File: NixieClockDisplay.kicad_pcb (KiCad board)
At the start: 2 copper layers, 160 x 65 mm, 61 parts, among them J1 CONN_01X08, J2 CONN_01X03, J3 CONN_01X03, J4 CONN_02X04, J5 CONN_01X02, U1 TPIC6B595, U2 TPIC6B595, U3 TPIC6B595, U4 TPIC6B595, U5 TPIC6B595, U6 TPIC6B595, U7 WE-FDSM_DC/DC_5V

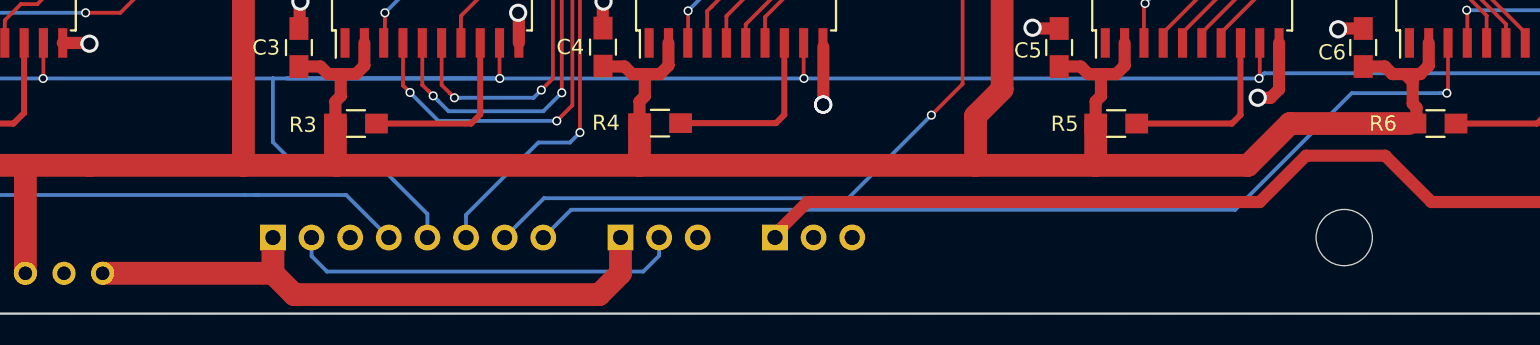
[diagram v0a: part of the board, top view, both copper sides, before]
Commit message: Arranged connectors to mate with NixiePowerSupply board.
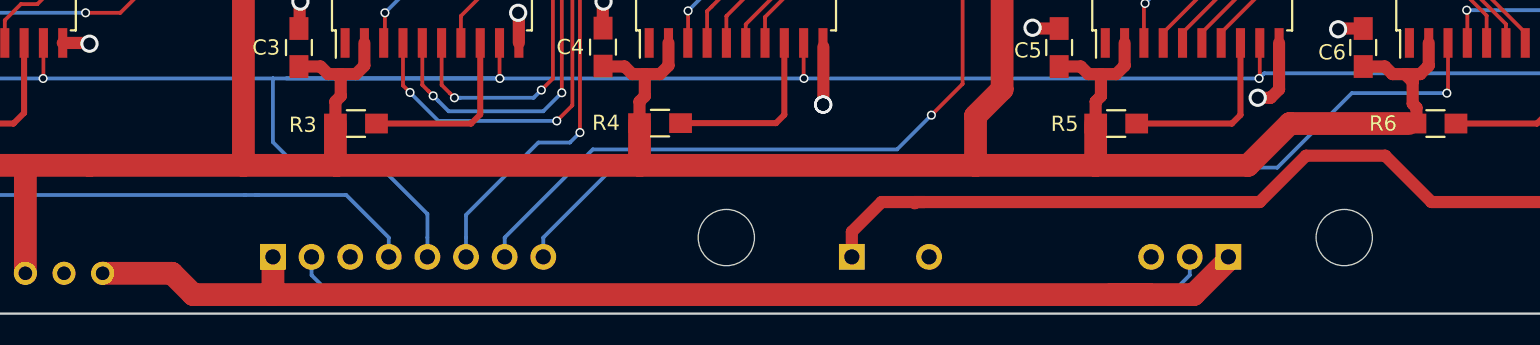
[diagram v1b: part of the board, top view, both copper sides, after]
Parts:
- added REF**: MountingHole_3.7mm, Mounting_Holes:MountingHole_3.7mm, F.Cu at (159.4, 100.0)
- J3: value CONN_01X03 -> CONN_01X02; footprint Pin_Headers:Pin_Header_Straight_1x03_Pitch2.54mm -> NixieClockDisplay:Pin_Header_Straight_1x03_Pitch2.54mm_No_Center
- moved J2 40.0 mm to (192.4, 101.3), turned to 90 degrees
- moved J3 5.21 mm to (167.6, 101.3)
- moved J1 1.27 mm to (129.5, 101.3)
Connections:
- J3 pad 2: Net-(J3-Pad2) -> GND
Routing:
- net +12V: track 39.9 -> 80.7 mm
- net /SHDN: track 26.1 -> 61.7 mm
- net /HV: track 325.0 -> 322.1 mm
- net Net-(J1-Pad8): track 66.7 -> 68.0 mm
- net /PIXEL_IN: track 101.9 -> 103.1 mm
- net /SRCK: track 182.1 -> 183.3 mm
- net /RCK: track 160.4 -> 161.7 mm
- net //G: track 166.2 -> 167.5 mm

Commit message: Final board.
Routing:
- net GND: track 155.5 -> 162.4 mm
- net Net-(LED2-Pad1): track 16.6 -> 14.0 mm
- net Net-(LED6-Pad1): track 16.3 -> 14.0 mm
- net Net-(LED1-Pad1): track 20.3 -> 18.4 mm
- net Net-(LED5-Pad1): track 20.2 -> 18.9 mm
- net Net-(LED10-Pad3): track 19.9 -> 18.7 mm
- net Net-(LED8-Pad1): track 16.2 -> 16.9 mm
- net Net-(LED4-Pad1): track 16.2 -> 16.9 mm
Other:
- board text added: "HV /EN"
- board text added: "NIXIE /EN"
- board text removed: "ENABLE"

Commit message: Begin layout
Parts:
- removed J1: CONN_01X08, Pin_Headers:Pin_Header_Straight_1x08_Pitch2.54mm
- removed the REF** at (159.4, 100.0)
- added C17: .01uF, Capacitors_SMD:C_0805_HandSoldering, F.Cu at (114.1, 99.5)
- added C18: .01uF, Capacitors_SMD:C_0805_HandSoldering, F.Cu at (106.7, 99.8)
- added C19: .1uF, Capacitors_SMD:C_0805_HandSoldering, F.Cu at (136.5, 107.0)
- added C20: .01uF, Capacitors_SMD:C_0805_HandSoldering, F.Cu at (120.2, 100.0)
- added R14: 10K, Resistors_SMD:R_0805_HandSoldering, F.Cu at (161.2, 98.8)
- added R15: 10K, Resistors_SMD:R_0805_HandSoldering, F.Cu at (161.2, 105.2)
- added R16: 10K, Resistors_SMD:R_0805_HandSoldering, F.Cu at (117.1, 99.7)
- added R17: 10K, Resistors_SMD:R_0805_HandSoldering, F.Cu at (109.4, 99.8)
- added R18: 10K, Resistors_SMD:R_0805_HandSoldering, F.Cu at (125.8, 100.0)
- added R19: 100, Resistors_SMD:R_0805_HandSoldering, F.Cu at (129.5, 100.0)
- added R20: 33R, Resistors_SMD:R_0805_HandSoldering, F.Cu at (135.0, 97.5)
- added R21: 10K, Resistors_SMD:R_0805_HandSoldering, F.Cu at (123.0, 100.0)
- added SW1: RotaryEncoder_Switch_RGB, NixieClockDisplay:EC12PLRGB_Rotary_Encoder, F.Cu at (150.0, 102.5)
- added U8: AdafruitProTrinket5V, NixieClockDisplay:Adafruit_Trinket_Pro, B.Cu at (150.0, 82.5)
- added U9: WS2811, Housings_SOIC:SOIC-8_3.9x4.9mm_Pitch1.27mm, F.Cu at (136.2, 102.1)
- J4: value CONN_02X04 -> Conn_02x02_Odd_Even; footprint Pin_Headers:Pin_Header_Straight_2x04_Pitch2.54mm -> Pin_Headers:Pin_Header_Straight_2x02_Pitch2.54mm
- J5: value CONN_01X02 -> Conn_01x04; footprint Pin_Headers:Pin_Header_Straight_1x02_Pitch2.54mm -> Pin_Headers:Pin_Header_Straight_1x04_Pitch2.54mm
- R10, R11, R12, R13, R8, R9: value 10K -> 22K
- moved U7 95.2 mm to (211.0, 97.5)
- moved C4 29.1 mm to (177.2, 74.5), turned to 180 degrees
- moved R4 21.5 mm to (176.5, 92.5)
- moved U3 21.0 mm to (119.0, 82.5), turned to 0 degrees
- moved U4 21.0 mm to (181.0, 82.5), turned to 0 degrees
- moved C5 18.4 mm to (194.2, 74.5), turned to 180 degrees
- moved C6 16.4 mm to (211.2, 74.5), turned to 180 degrees
- moved R1 11.2 mm to (76.2, 85.5), turned to 90 degrees
- moved C2 10.4 mm to (94.0, 80.0), turned to 90 degrees
- moved C1 9.01 mm to (76.2, 80.0), turned to 90 degrees
- moved U2 8.00 mm to (102.0, 82.5), turned to 0 degrees
- moved U5 8.00 mm to (198.0, 82.5), turned to 0 degrees
- moved R6 6.18 mm to (212.0, 91.0), turned to 180 degrees
- moved U1 5.00 mm to (85.0, 82.5), turned to 0 degrees
- moved U6 5.00 mm to (215.0, 82.5), turned to 0 degrees
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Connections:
- net /HV renamed Net-(J3-Pad1)
- J4 pad 1: /PIXEL_IN -> Net-(J4-Pad1)
- J4 pad 3: /RING_OUT -> +5V
- J4 pad 4: /RING_IN -> GND
- J5 pad 2: GND -> /TIME_IN
- N1 pad 8: Net-(N1-Pad8) -> /HOUR_40
- N1 pad 9: Net-(N1-Pad9) -> /HOUR_30
- R1 pad 1: +5V -> Net-(R1-Pad1)
- R1 pad 2: Net-(R1-Pad2) -> +5V
- R2 pad 1: +5V -> Net-(R2-Pad1)
- R2 pad 2: Net-(R2-Pad2) -> +5V
- R3 pad 1: +5V -> Net-(R3-Pad1)
- R3 pad 2: Net-(R3-Pad2) -> +5V
- R4 pad 1: +5V -> Net-(R4-Pad1)
- R4 pad 2: Net-(R4-Pad2) -> +5V
- R5 pad 1: +5V -> Net-(R5-Pad1)
- R5 pad 2: Net-(R5-Pad2) -> +5V
- R6 pad 1: +5V -> Net-(R6-Pad1)
- R6 pad 2: Net-(R6-Pad2) -> +5V
- R7 pad 2: Net-(J4-Pad2) -> Net-(R7-Pad2)
- U1 pad 16: Net-(U1-Pad16) -> /HOUR_30
- U1 pad 17: Net-(U1-Pad17) -> /HOUR_40
- U1 pad 8: Net-(R1-Pad2) -> Net-(R1-Pad1)
- U2 pad 8: Net-(R2-Pad2) -> Net-(R2-Pad1)
- U3 pad 8: Net-(R3-Pad2) -> Net-(R3-Pad1)
- U4 pad 8: Net-(R4-Pad2) -> Net-(R4-Pad1)
- U5 pad 8: Net-(R5-Pad2) -> Net-(R5-Pad1)
- U6 pad 8: Net-(R6-Pad2) -> Net-(R6-Pad1)
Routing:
- net +5V: track 532.5 -> 300.3 mm, vias 10 -> 8
- net /PIXEL_IN: track 103.1 -> 0.00 mm, vias 1 -> 0
- net /MIN_9: track 81.7 -> 0.00 mm, vias 2 -> 0
- net +12V: track 80.7 -> 0.00 mm
- net /MIN_8: track 75.9 -> 0.00 mm, vias 2 -> 0
- net /HOUR_9: track 73.4 -> 0.00 mm, vias 2 -> 0
- net /MIN_7: track 69.9 -> 0.00 mm, vias 2 -> 0
- net Net-(U6-Pad3): track 68.0 -> 0.00 mm, vias 1 -> 0
- net /HOUR_8: track 66.8 -> 0.00 mm, vias 2 -> 0
- net /SEC_60: track 65.6 -> 0.00 mm, vias 2 -> 0
- net /SHDN: track 61.7 -> 0.00 mm
- net /HOUR_7: track 60.9 -> 0.00 mm, vias 2 -> 0
- net /MIN_50: track 54.4 -> 0.00 mm, vias 2 -> 0
- net /SEC_8: track 50.6 -> 0.00 mm
- net /SEC_9: track 47.0 -> 0.00 mm, vias 2 -> 0
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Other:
- board size 160 x 65 mm -> 160 x 70 mm
- board text added: "DOUT to ring DIN Ring DOUT to DIN Short DOUT-DIN to omit ring"
- board text added: "TIME IN"
- board text removed: "1"
- board text removed: "2"
- board text removed: "3"
- board text removed: "HV /EN"
- board text removed: "NIXIE /EN"
- board text removed: "NIXIE DIN"
- board text removed: "PIXEL DIN"
- board text removed: "RCK"
- board text removed: "SRCK"
- board text removed: "Shunt 1-2 to omit ring Shunt 1-3 and 2-4 for ring DOUT to ring DIN Ring DOUT to DIN"

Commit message: More layout
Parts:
- moved C3 22.0 mm to (115.2, 74.5), turned to 180 degrees
- moved R3 18.9 mm to (115.5, 91.2), turned to 180 degrees
- moved R5 9.58 mm to (194.5, 91.2), turned to 180 degrees
- moved R1 7.79 mm to (81.5, 91.2), turned to 180 degrees
- moved R2 7.60 mm to (98.5, 91.2), turned to 180 degrees
- moved C1 7.43 mm to (81.2, 74.5), turned to 180 degrees
- moved C2 6.95 mm to (98.2, 74.5), turned to 180 degrees
- moved R4 1.56 mm to (177.5, 91.2), turned to 180 degrees
- moved R6 0.56 mm to (211.5, 91.2)
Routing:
- net +5V: track 300.3 -> 400.1 mm, vias 8 -> 18
- net /MIN_8: track 0.00 -> 86.1 mm, vias 0 -> 2
- net /MIN_9: track 0.00 -> 79.3 mm, vias 0 -> 2
- net Net-(U3-Pad3): track 0.00 -> 76.0 mm, vias 0 -> 2
- net /MIN_4: track 0.00 -> 69.1 mm, vias 0 -> 1
- net /MIN_5: track 0.00 -> 64.9 mm, vias 0 -> 1
- net /MIN_6: track 0.00 -> 56.3 mm, vias 0 -> 1
- net /MIN_3: track 0.00 -> 52.8 mm, vias 0 -> 1
- net /SEC_8: track 0.00 -> 51.2 mm, vias 0 -> 2
- net /SEC_60: track 0.00 -> 45.7 mm
- net /SEC_40: track 0.00 -> 45.5 mm
- net /SEC_9: track 0.00 -> 44.9 mm, vias 0 -> 2
- net /SEC_50: track 0.00 -> 44.3 mm
- net /MIN_2: track 0.00 -> 39.4 mm
- net /SEC_30: track 0.00 -> 38.1 mm
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
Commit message: More layout
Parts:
- moved C18 52.5 mm to (155.8, 81.0)
- moved R17 52.3 mm to (158.2, 81.0)
- moved C20 47.0 mm to (163.2, 81.0), turned to 270 degrees
- moved R21 42.3 mm to (160.8, 81.0), turned to 270 degrees
- moved C17 41.1 mm to (150.8, 81.0)
- moved R16 40.7 mm to (153.2, 81.0)
- moved C19 1.75 mm to (134.8, 107.0)
- moved R14 1.27 mm to (161.5, 100.0), turned to 180 degrees
- moved R15 0.35 mm to (161.5, 105.0), turned to 180 degrees
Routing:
- net +5V: track 400.1 -> 494.2 mm, vias 18 -> 23
- net /MIN_7: track 0.00 -> 83.3 mm, vias 0 -> 2
- net /MIN_50: track 0.00 -> 71.7 mm, vias 0 -> 3
- net /MIN_00: track 0.00 -> 49.9 mm, vias 0 -> 1
- net Net-(R15-Pad2): track 0.00 -> 41.3 mm
- net Net-(R14-Pad2): track 0.00 -> 30.0 mm
- net /HOUR_0: track 0.00 -> 29.7 mm, vias 0 -> 2
- net /HOUR_2: track 0.00 -> 25.3 mm
- net /HOUR_20: track 0.00 -> 23.5 mm, vias 0 -> 2
- net /HOUR_1: track 0.00 -> 22.7 mm, vias 0 -> 2
- net /HOUR_10: track 0.00 -> 19.1 mm
- net Net-(C20-Pad1): track 0.00 -> 10.3 mm
- net Net-(C18-Pad1): track 0.00 -> 8.21 mm
- net Net-(R2-Pad1): track 0.00 -> 7.73 mm
- net Net-(R1-Pad1): track 0.00 -> 7.73 mm
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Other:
- board text added: "WWVB IN"
- board text removed: "TIME IN"

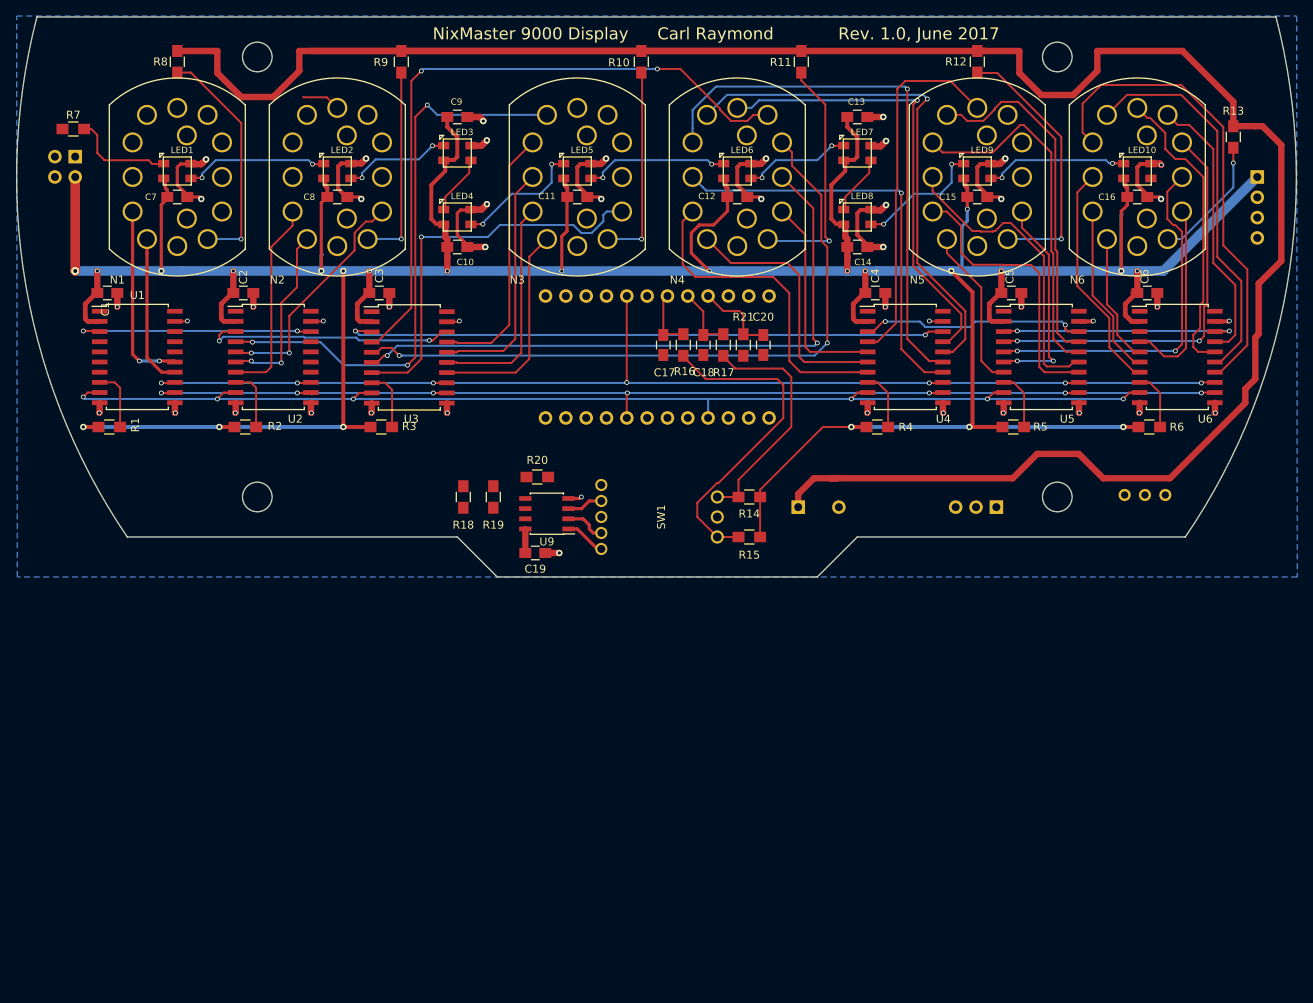
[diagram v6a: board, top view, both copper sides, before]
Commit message: Add Adafruit Trinket Pro, rotary switch
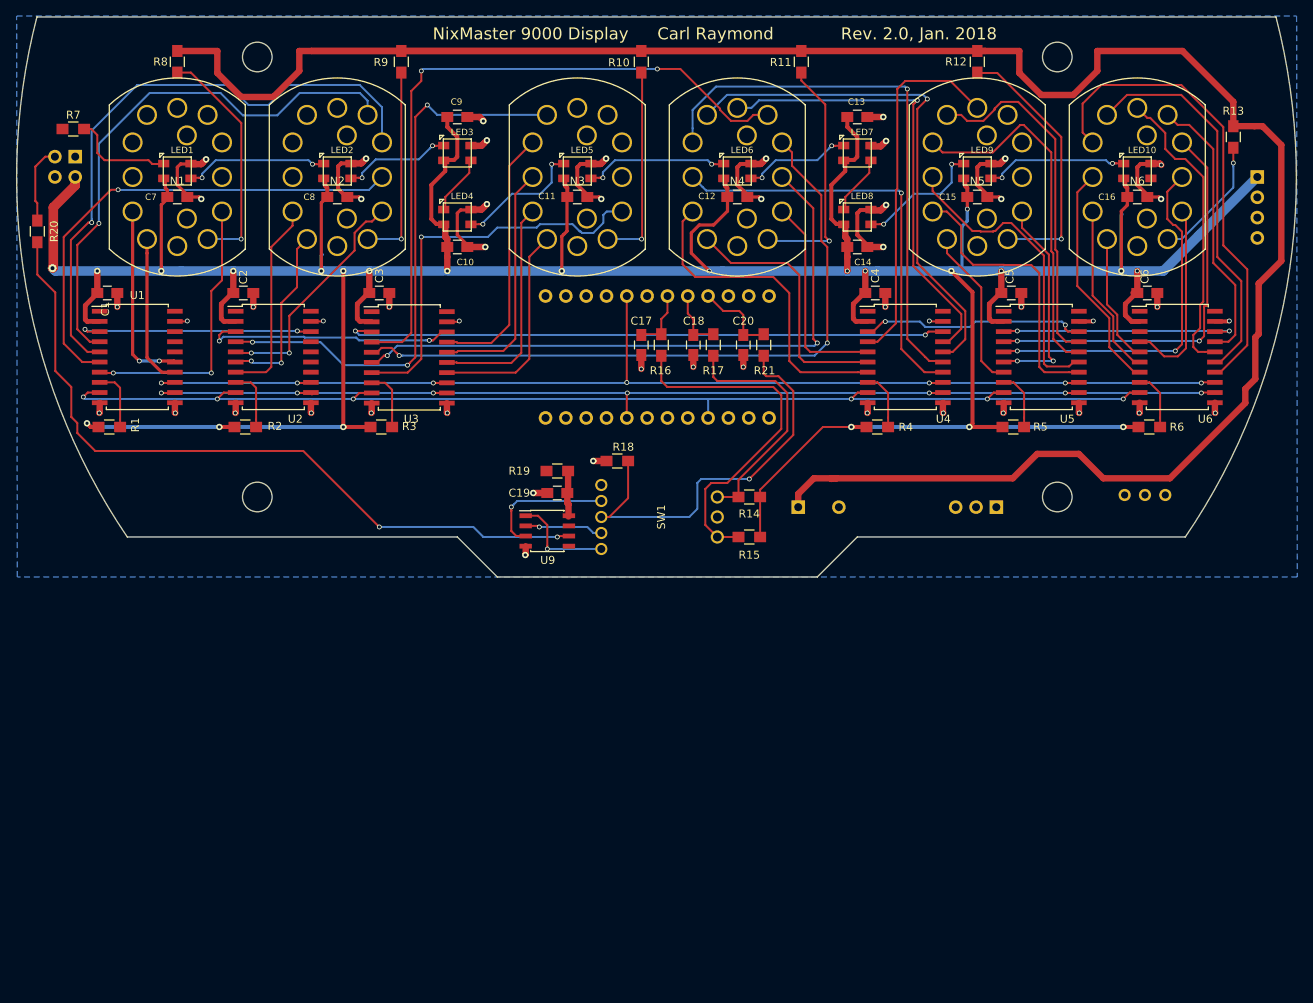
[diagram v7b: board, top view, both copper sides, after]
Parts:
- moved R20 69.6 mm to (72.5, 66.8), turned to 270 degrees
- moved R18 19.8 mm to (145.0, 95.5), turned to 0 degrees
- moved R19 8.63 mm to (137.5, 96.8), turned to 180 degrees
- moved C19 7.99 mm to (137.5, 99.5), turned to 180 degrees
- moved C17 2.75 mm to (148.0, 81.0)
- moved R16 2.75 mm to (150.5, 81.0)
- moved R21 2.55 mm to (163.3, 81.0)
- moved C20 2.50 mm to (160.8, 81.0)
- moved U9 2.16 mm to (136.2, 104.2), turned to 0 degrees
- moved C18 1.25 mm to (154.5, 81.0)
- moved R17 1.25 mm to (157.0, 81.0)
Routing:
- net Net-(R20-Pad2): track 0.00 -> 92.8 mm, vias 0 -> 2
- net /HOUR_8: track 0.00 -> 77.6 mm, vias 0 -> 1
- net /HOUR_7: track 0.00 -> 68.5 mm, vias 0 -> 1
- net /HOUR_9: track 0.00 -> 61.7 mm, vias 0 -> 1
- net Net-(R18-Pad2): track 0.00 -> 51.5 mm, vias 0 -> 1
- net /HOUR_00: track 0.00 -> 34.7 mm, vias 0 -> 2
- net Net-(SW1-Pad4): track 4.50 -> 16.7 mm, vias 0 -> 1
- net Net-(J4-Pad2): track 0.00 -> 9.81 mm
- net Net-(SW1-Pad1): track 5.14 -> 13.4 mm, vias 0 -> 1
- net GND: track 129.0 -> 134.5 mm, vias 46 -> 50
- net /HOUR_6: track 4.81 -> 0.00 mm
- net Net-(SW1-Pad2): track 5.13 -> 9.82 mm, vias 0 -> 1
- net Net-(R15-Pad2): track 41.3 -> 44.9 mm
- net +5V: track 494.2 -> 497.5 mm
- net Net-(C19-Pad1): track 3.00 -> 5.79 mm
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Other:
- board text added: "Rev. 2.0, Jan. 2018"
- board text removed: "Rev. 1.0, June 2017"
